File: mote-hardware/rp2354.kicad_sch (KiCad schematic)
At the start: 31 parts, among them J4 SM03B-SRSS-TB, SW1 SW_Push, SW2 SW_Push, U1 RP2350_60QFN, U4 RP Radio Module 2, Y1 ABM8-272-T3

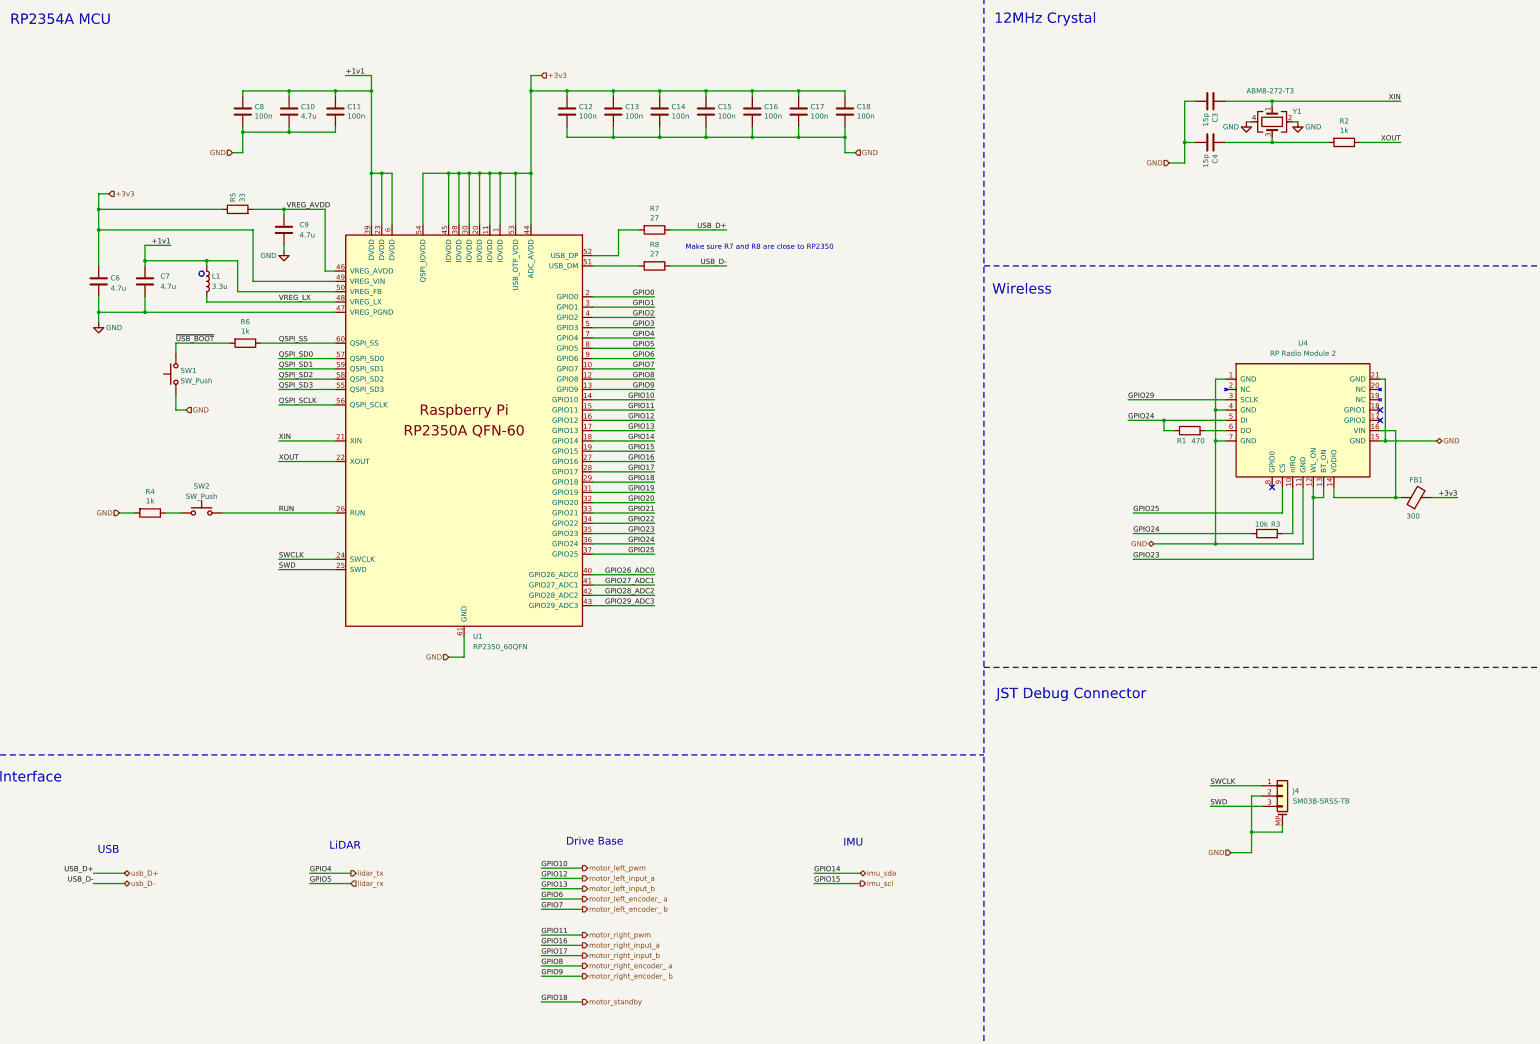
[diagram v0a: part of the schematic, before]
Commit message: Implement motor, power, imu, status LED schematics
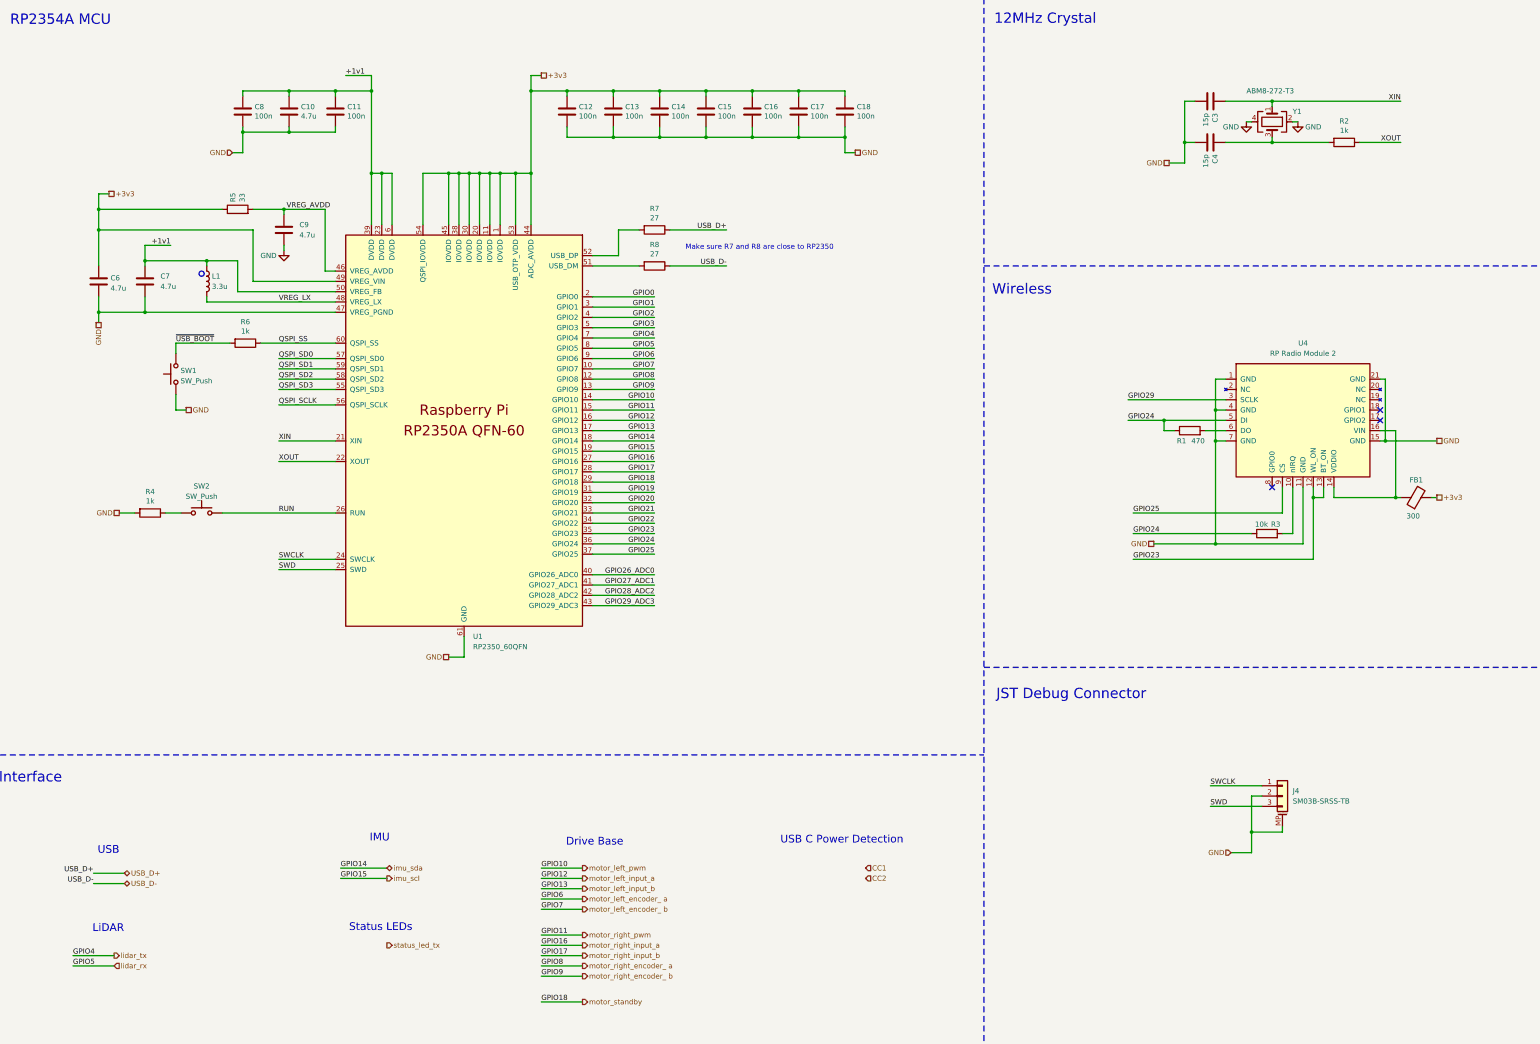
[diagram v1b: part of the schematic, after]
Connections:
- net usb_D+ renamed USB_D+
- net usb_D- renamed USB_D-
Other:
- note added: "Status LEDs"
- note added: "USB C Power Detection"
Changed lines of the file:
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@@
 		)
 	)
+	(text "USB C Power Detection"
+		(exclude_from_sim no)
+		(at 222.758 221.488 0)
+		(effects
+			(font
+				(size 1.905 1.905)
+			)
+			(justify bottom)
+		)
+	)
 	(text "USB"
 		(exclude_from_sim no)
@@
 	(text "IMU"
 		(exclude_from_sim no)
-		(at 225.552 222.25 0)
+		(at 108.712 220.98 0)
 		(effects
 			(font
@@
 		)
 	)
+	(text "Status LEDs"
+		(exclude_from_sim no)
+		(at 108.966 243.078 0)
+		(effects
+			(font
+				(size 1.905 1.905)
+			)
+			(justify bottom)
+		)
+	)
 	(text "LiDAR"
 		(exclude_from_sim no)
-		(at 96.266 223.012 0)
+		(at 37.846 243.332 0)
 		(effects
 			(font
@@
 	(wire
 		(pts
-			(xy 91.44 231.14) (xy 101.6 231.14)
+			(xy 33.02 251.46) (xy 43.18 251.46)
 		)
 		(stroke
@@
 	(wire
 		(pts
-			(xy 215.9 231.14) (xy 227.33 231.14)
+			(xy 99.06 229.87) (xy 110.49 229.87)
 		)
 		(stroke
@@
 	(wire
 		(pts
-			(xy 91.44 228.6) (xy 101.6 228.6)
+			(xy 33.02 248.92) (xy 43.18 248.92)
 		)
 		(stroke
@@
 	(wire
 		(pts
-			(xy 215.9 228.6) (xy 227.33 228.6)
+			(xy 99.06 227.33) (xy 110.49 227.33)
 		)
 		(stroke
@@
 	(wire
 		(pts
-			(xy 368.3 135.89) (xy 374.65 135.89)
+			(xy 368.3 135.89) (xy 369.57 135.89)
 		)
 		(stroke
@@
 	)
 	(label "GPIO15"
-		(at 215.9 231.14 0)
+		(at 99.06 229.87 0)
 		(effects
 			(font
@@
 	)
 	(label "GPIO14"
-		(at 215.9 228.6 0)
+		(at 99.06 227.33 0)
 		(effects
 			(font
@@
 		)
 	)
-	(label "+3v3"
-		(at 374.65 135.89 180)
-		(effects
-			(font
-				(size 1.27 1.27)
-			)
-			(justify right bottom)
-		)
-	)
 	(label "RUN"
 		(at 83.82 139.7 0)
@@
 	)
 	(label "GPIO4"
-		(at 91.44 228.6 0)
+		(at 33.02 248.92 0)
 		(effects
 			(font
@@
 	)
 	(label "GPIO5"
-		(at 91.44 231.14 0)
+		(at 33.02 251.46 0)
 		(effects
 			(font
@@
 	)
 	(hierarchical_label "GND"
-		(shape input)
+		(shape passive)
 		(at 226.06 50.8 0)
 		(effects
@@
 	)
 	(hierarchical_label "GND"
-		(shape input)
+		(shape passive)
 		(at 303.53 53.34 180)
 		(effects
@@
 	(hierarchical_label "lidar_rx"
 		(shape input)
-		(at 101.6 231.14 0)
+		(at 43.18 251.46 0)
+		(effects
+			(font
+				(size 1.27 1.27)
+			)
+			(justify left)
+		)
+	)
+	(hierarchical_label "CC1"
+		(shape input)
+		(at 228.6 227.33 0)
 		(effects
 			(font
@@
 	)
 	(hierarchical_label "GND"
-		(shape bidirectional)
+		(shape passive)
 		(at 299.72 147.32 180)
 		(effects
@@
 	)
 	(hierarchical_label "GND"
-		(shape bidirectional)
+		(shape passive)
 		(at 369.57 121.92 0)
 		(effects
@@
 		)
 	)
-	(hierarchical_label "usb_D-"
+	(hierarchical_label "USB_D-"
 		(shape bidirectional)
 		(at 45.72 231.14 0)
@@
 		)
 	)
-	(hierarchical_label "usb_D+"
+	(hierarchical_label "USB_D+"
 		(shape bidirectional)
 		(at 45.72 228.6 0)
@@
 	)
 	(hierarchical_label "+3v3"
-		(shape input)
+		(shape passive)
 		(at 148.59 31.75 0)
 		(effects
@@
 	(hierarchical_label "imu_scl"
 		(shape output)
-		(at 227.33 231.14 0)
+		(at 110.49 229.87 0)
 		(effects
 			(font
@@
 	(hierarchical_label "lidar_tx"
 		(shape output)
-		(at 101.6 228.6 0)
+		(at 43.18 248.92 0)
 		(effects
 			(font
@@
 	)
 	(hierarchical_label "GND"
-		(shape input)
+		(shape passive)
 		(at 125.73 175.26 180)
 		(effects
@@
 	)
 	(hierarchical_label "GND"
-		(shape input)
+		(shape passive)
+		(at 39.37 92.71 270)
+		(effects
+			(font
+				(size 1.27 1.27)
+			)
+			(justify right)
+		)
+	)
+	(hierarchical_label "GND"
+		(shape passive)
 		(at 60.96 114.3 0)
 		(effects
@@
 		)
 	)
+	(hierarchical_label "status_led_tx"
+		(shape output)
+		(at 110.49 246.38 0)
+		(effects
+			(font
+				(size 1.27 1.27)
+			)
+			(justify left)
+		)
+	)
 	(hierarchical_label "+3v3"
-		(shape input)
+		(shape passive)
 		(at 41.91 60.96 0)
 		(effects
@@
 		)
 	)
+	(hierarchical_label "CC2"
+		(shape input)
+		(at 228.6 229.87 0)
+		(effects
+			(font
+				(size 1.27 1.27)
+			)
+			(justify left)
+		)
+	)
 	(hierarchical_label "imu_sda"
 		(shape bidirectional)
-		(at 227.33 228.6 0)
+		(at 110.49 227.33 0)
 		(effects
 			(font
@@
 	)
 	(hierarchical_label "GND"
-		(shape input)
+		(shape passive)
 		(at 44.45 139.7 180)
 		(effects
@@
 		)
 	)
+	(hierarchical_label "+3v3"
+		(shape passive)
+		(at 369.57 135.89 0)
+		(effects
+			(font
+				(size 1.27 1.27)
+			)
+			(justify left)
+		)
+	)
 	(symbol
 		(lib_id "Device:R")
@@
 					(unit 1)
 				)
-			)
-		)
-	)
-	(symbol
-		(lib_id "power:GND")
-		(at 39.37 92.71 0)
-		(mirror y)
-		(unit 1)
-		(exclude_from_sim no)
-		(in_bom yes)
-		(on_board yes)
-		(dnp no)
-		(property "Reference" "#PWR014"
-			(at 39.37 99.06 0)
-			(effects
-				(font
-					(size 1.27 1.27)
-				)
-				(hide yes)
-			)
-		)
-		(property "Value" "GND"
-			(at 43.18 93.98 0)
-			(effects
-				(font
-					(size 1.27 1.27)
-				)
-			)
-		)
-		(property "Footprint" ""
-			(at 39.37 92.71 0)
-			(effects
-				(font
-					(size 1.27 1.27)
-				)
-				(hide yes)
-			)
-		)
-		(property "Datasheet" ""
-			(at 39.37 92.71 0)
-			(effects
-				(font
-					(size 1.27 1.27)
-				)
-				(hide yes)
-			)
-		)
-		(property "Description" ""
-			(at 39.37 92.71 0)
-			(effects
-				(font
-					(size 1.27 1.27)
-				)
-			)
-		)
-		(pin "1"
-		)
-		(instances
-			(project "mote-hardware"
-				(path "/94683f5c-9cd9-448e-be96-9792537b5cb8/8aa6d869-37ab-4fd7-8af1-9416ab877c54"
-					(reference "#PWR014")
-					(unit 1)
-				)

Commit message: First draft schematic complete
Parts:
- added J6: Conn_01x03_Pin, symbol Connector:Conn_01x03_Pin
- U1: footprint RP2350_60QFN_minimal:RP2350-QFN-60-1EP_7x7_P0.4mm_EP3.4x3.4mm_ThermalVias -> RP2354_60QFN_minimal:RP2350-QFN-60-1EP_7x7_P0.4mm_EP3.4x3.4mm_ThermalVias; symbol MCU_RaspberryPi_RP2350:RP2350_60QFN -> MCU_RaspberryPi_RP2350:RP2354_60QFN
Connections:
- net GPIO19 is gone; now on net status_led_tx: U1.31 (GPIO19)
- net GPIO26_ADC0 is gone; now on net CC1: U1.40 (GPIO26_ADC0)
- net GPIO27_ADC1 is gone; now on net CC2: U1.41 (GPIO27_ADC1)
- net motor_left_pwm is gone; now on net motor_left_input_a: U1.14 (GPIO10)
- net motor_right_pwm is gone; now on net motor_left_input_b: U1.15 (GPIO11)
- net GND: now also J6.2 (Pin_2)
- net SWCLK: now also J6.3 (Pin_3)
- net SWD: now also J6.1 (Pin_1)
- net motor_left_input_a: no longer U1.16 (GPIO12)
- net motor_left_input_b: no longer U1.17 (GPIO13)
- net motor_right_input_a: now also U1.16 (GPIO12); no longer U1.27 (GPIO16)
- net motor_right_input_b: now also U1.17 (GPIO13); no longer U1.28 (GPIO17)
- net motor_left_encoder_ a renamed motor_left_encoder_a
- net motor_left_encoder_ b renamed motor_left_encoder_b
- net motor_right_encoder_ a renamed motor_right_encoder_a
- net motor_right_encoder_ b renamed motor_right_encoder_b
- new net GPIO16: U1.27 (GPIO16)
- new net GPIO17: U1.28 (GPIO17)
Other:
- note added: "Debug Connectors"
- note removed: "JST Debug Connector"
- company: (none) -> github.com/usedhondacivic/mote
- title: (none) -> Mote
- moved on the sheet: J4

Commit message: Footprint assignments
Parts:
- FB1: footprint (none) -> Inductor_SMD:L_0805_2012Metric
- J6: footprint (none) -> Connector_PinHeader_2.54mm:PinHeader_1x03_P2.54mm_Vertical
- R1, R3: footprint (none) -> Resistor_SMD:R_0402_1005Metric
- U1: footprint RP2354_60QFN_minimal:RP2350-QFN-60-1EP_7x7_P0.4mm_EP3.4x3.4mm_ThermalVias -> RP2350_60QFN_minimal:RP2350-QFN-60-1EP_7x7_P0.4mm_EP3.4x3.4mm_ThermalVias
- U4: footprint (none) -> mote-hardware:rpi_rmc20452t
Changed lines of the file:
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@@
 			)
 		)
-		(property "Footprint" ""
+		(property "Footprint" "Inductor_SMD:L_0805_2012Metric"
 			(at 364.49 137.668 90)
 			(effects
@@
 			)
 		)
-		(property "Footprint" "RP2354_60QFN_minimal:RP2350-QFN-60-1EP_7x7_P0.4mm_EP3.4x3.4mm_ThermalVias"
+		(property "Footprint" "RP2350_60QFN_minimal:RP2350-QFN-60-1EP_7x7_P0.4mm_EP3.4x3.4mm_ThermalVias"
 			(at 110.49 119.38 0)
 			(effects
@@
 			)
 		)
-		(property "Footprint" ""
+		(property "Footprint" "Connector_PinHeader_2.54mm:PinHeader_1x03_P2.54mm_Vertical"
 			(at 355.6 214.63 0)
 			(effects
@@
 			)
 		)
-		(property "Footprint" ""
+		(property "Footprint" "Resistor_SMD:R_0402_1005Metric"
 			(at 327.66 146.558 90)
 			(effects
@@
 			)
 		)
-		(property "Footprint" ""
+		(property "Footprint" "mote-hardware:rpi_rmc20452t"
 			(at 335.28 128.27 0)
 			(effects
@@
 			)
 		)
-		(property "Footprint" ""
+		(property "Footprint" "Resistor_SMD:R_0402_1005Metric"
 			(at 308.61 121.158 90)
 			(effects
